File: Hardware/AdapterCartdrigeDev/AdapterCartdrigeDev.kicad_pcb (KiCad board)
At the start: 2 copper layers, 30.1 x 43.4 mm, 3 parts, among them J1 ROM, U1 28C256

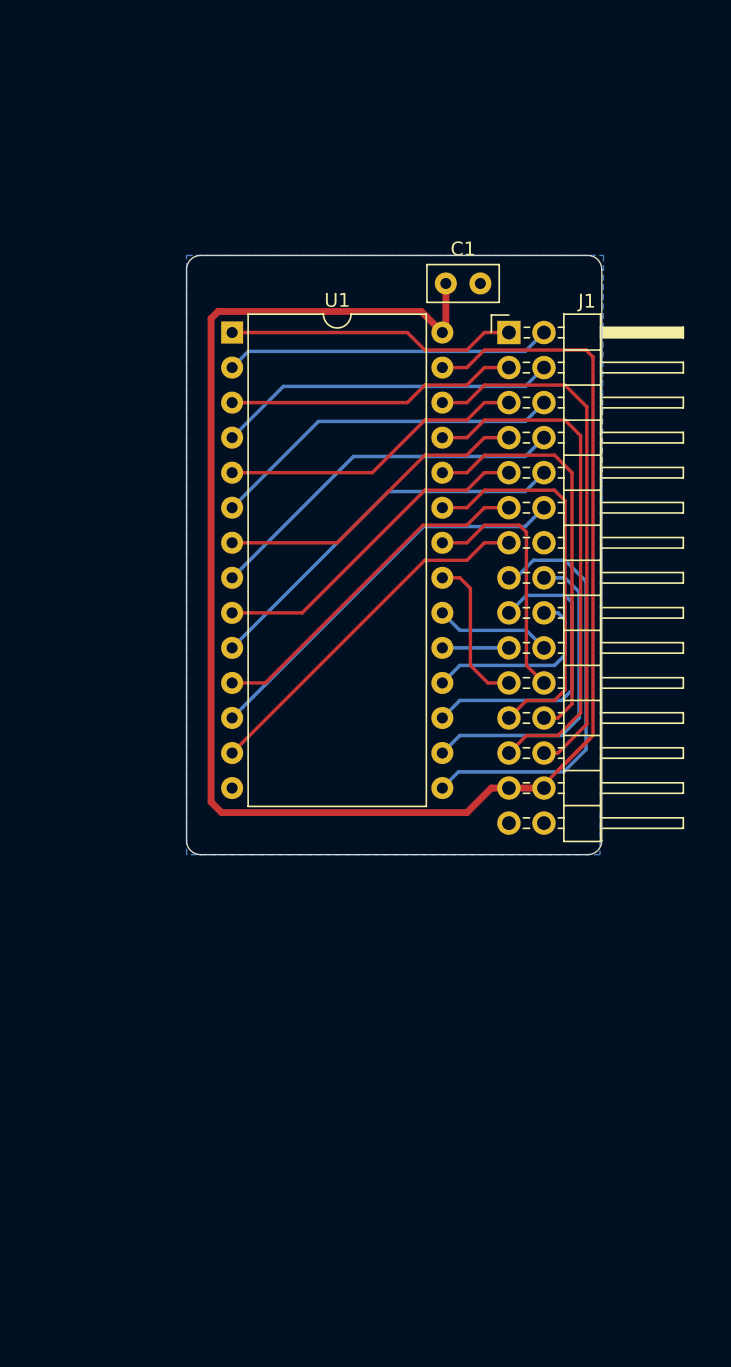
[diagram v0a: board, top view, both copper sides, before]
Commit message: New PLD logic, VGA, DMA ...
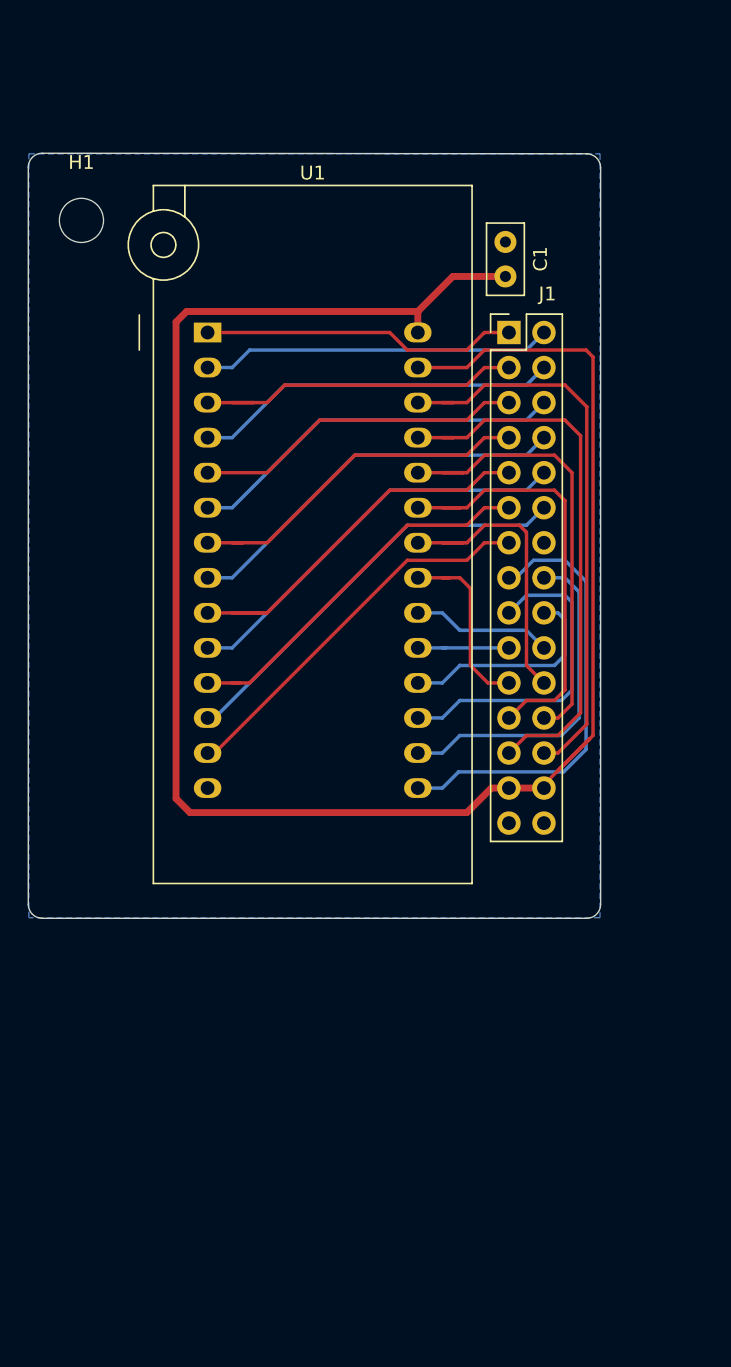
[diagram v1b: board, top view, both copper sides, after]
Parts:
- added H1: MountingHole_Pad, MountingHole:MountingHole_3.2mm_M3, F.Cu at (90.9, 42.9)
- J1: footprint Connector_PinHeader_2.54mm:PinHeader_2x15_P2.54mm_Horizontal -> Connector_PinHeader_2.54mm:PinHeader_2x15_P2.54mm_Vertical
- U1: footprint Package_DIP:DIP-28_W15.24mm -> Socket:DIP_Socket-28_W11.9_W12.7_W15.24_W17.78_W18.5_3M_228-1277-00-0602J
- moved C1 4.35 mm to (121.7, 47.0), turned to 90 degrees
- moved U1 1.78 mm to (100.1, 51.1)
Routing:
- net +5V: track 129.1 -> 138.5 mm
- net /A1: track 24.3 -> 28.6 mm
- net /A7: track 21.1 -> 24.4 mm
- net /A9: track 29.7 -> 33.0 mm
- net OE: track 18.3 -> 21.6 mm
- net /A11: track 28.4 -> 31.4 mm
- net /A3: track 23.2 -> 25.8 mm
- net /A8: track 37.5 -> 40.0 mm
- net /A13: track 38.6 -> 41.2 mm
- net /D0: track 25.3 -> 27.6 mm
- net /A10: track 11.3 -> 13.5 mm
- net /D7: track 4.83 -> 6.86 mm
- net /A4: track 25.8 -> 27.5 mm
- net /A5: track 22.2 -> 23.9 mm
- net /A14: track 21.1 -> 22.9 mm
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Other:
- board size 30.1 x 43.4 mm -> 41.5 x 55.5 mm

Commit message: Fix
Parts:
- added H2: MountingHole_Pad, MountingHole:MountingHole_3.2mm_M3, F.Cu at (96.0, 119.0)
- added H3: MountingHole_Pad, MountingHole:MountingHole_3.2mm_M3, F.Cu at (131.0, 34.0)
- added XiaoNiuNiu: LOGO, Logos:VerySmallCow, F.Cu at (129.5, 118.1)
- moved H1 10.3 mm to (96.0, 34.0)
- moved J1 6.27 mm to (127.9, 49.3)
- moved C1 2.93 mm to (124.0, 45.2)
- moved U1 2.93 mm to (102.4, 49.3)
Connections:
- H1 pad : (no net) -> GND
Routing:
- net +5V: track 138.5 -> 142.4 mm
- net CS: track 10.2 -> 13.9 mm
- net /A14: track 22.9 -> 26.6 mm
- net /D4: track 24.8 -> 28.5 mm
- net /D5: track 23.7 -> 27.4 mm
- net /A0: track 29.6 -> 33.3 mm
- net /A5: track 23.9 -> 27.6 mm
- net /A2: track 28.6 -> 32.3 mm
- net /A4: track 27.5 -> 31.2 mm
- net /A6: track 26.5 -> 30.2 mm
- net /A12: track 25.4 -> 29.1 mm
- net /D6: track 15.8 -> 19.5 mm
- net /D7: track 6.86 -> 10.3 mm
- net /D0: track 27.6 -> 30.8 mm
- net /D2: track 28.2 -> 31.3 mm
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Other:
- board size 41.5 x 55.5 mm -> 45 x 95 mm
